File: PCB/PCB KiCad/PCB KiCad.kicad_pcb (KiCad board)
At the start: 2 copper layers, 80.1 x 120 mm, 78 parts, among them J1 Conn_01x04, J2 Conn_01x08, J3 Qwiic, J4 Conn_01x04, J5 Conn_01x04, SW1 MCU_RESET, SW2 TRIGGER, U1 OPA2376AID, U2 NAU7802SGI, U3 AMS1117-3.3, U4 TLC59208FIPWR

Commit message: typo
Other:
- board text added: "Plastic Scanner Development Board 2.3 May 2023"
- board text removed: "Plastic Scanner Development Board 2.2 April 2023"

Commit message: pre route
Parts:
- removed the ? at (119.0, 32.0)
- removed the ? at (47.0, 144.0)
- removed A1: Arduino_UNO_R3, Module:Arduino_UNO_R3
- removed C15: 22u, Capacitor_SMD:C_0805_2012Metric_Pad1.18x1.45mm_HandSolder
- removed C16: 100n, Capacitor_SMD:C_0805_2012Metric_Pad1.18x1.45mm_HandSolder
- removed D11: 1720nm, LED_SMD:LED_1206_3216Metric_Pad1.42x1.75mm_HandSolder
- removed D12: LED RED, LED_SMD:LED_0805_2012Metric_Pad1.15x1.40mm_HandSolder
- removed the D3 at (91.4, 33.4)
- removed the G*** at (118.9, 48.5)
- removed the G*** at (118.6, 40.5)
- removed the G*** at (83.4, 121.0)
- removed G1: LOGO, LOGO
- removed the J2 at (47.3, 119.2)
- removed R16, R17, R18, R19, R20, R21, R22: 47, Resistor_SMD:R_0805_2012Metric_Pad1.20x1.40mm_HandSolder
- removed the R7 at (88.2, 33.4)
- removed the R8 at (94.7, 33.4)
- removed REF**, e (x3): MountingHole_3.2mm_M3, MountingHole:MountingHole_3.2mm_M3
- removed SW1: MCU_RESET, Button_Switch_THT:SW_PUSH_6mm
- removed SW2: TRIGGER, Button_Switch_THT:SW_PUSH_6mm
- removed U4: TLC59208FIPWR, TLC59208:Texas_Instruments-TLC59208FIPWR-Level_A
- removed mouse-bite-2mm-slot (x6): VAL**, mousebites:mouse-bite-2mm-slot
- added ?: , , F.Cu at (97.9, 151.8)
- added ?: , , F.Cu at (67.9, 121.8)
- added ?: , , F.Cu at (67.9, 151.8)
- added C14: 100n, Capacitor_SMD:C_0805_2012Metric_Pad1.18x1.45mm_HandSolder, F.Cu at (65.2, 121.9)
- added D10: 1720nm, LED_SMD:LED_1206_3216Metric_Pad1.42x1.75mm_HandSolder, F.Cu at (78.4, 131.1)
- added H1: MountingHole, MountingHole:MountingHole_3.2mm_M3, F.Cu at (67.9, 121.8)
- added H2: MountingHole, MountingHole:MountingHole_3.2mm_M3, F.Cu at (67.9, 151.8)
- added H3: MountingHole, MountingHole:MountingHole_3.2mm_M3, F.Cu at (97.9, 151.8)
- added H4: MountingHole, MountingHole:MountingHole_3.2mm_M3, F.Cu at (97.9, 121.8)
- added J4: Conn_01x04, Connector_PinSocket_2.54mm:PinSocket_1x04_P2.54mm_Vertical, F.Cu at (65.2, 142.3)
- added R11: 47, Resistor_SMD:R_0805_2012Metric_Pad1.20x1.40mm_HandSolder, F.Cu at (96.0, 131.8)
- added R12: 47, Resistor_SMD:R_0805_2012Metric_Pad1.20x1.40mm_HandSolder, F.Cu at (96.0, 134.8)
- added R13: 47, Resistor_SMD:R_0805_2012Metric_Pad1.20x1.40mm_HandSolder, F.Cu at (96.0, 137.7)
- added R15: 47, Resistor_SMD:R_0805_2012Metric_Pad1.20x1.40mm_HandSolder, F.Cu at (96.0, 143.6)
- C1, C10, C11, C2, C3, C4, C5, C6, C7, C8, C9, FB1, R1, R2, R3, R4, R5, R6, U1, U2: moved to B.Cu
- C12: renamed from C14; moved to B.Cu
- C13: value 10u -> 22u
- D2: value LED BLUE -> LED RED; moved to B.Cu
- J2: renamed from J3; moved to B.Cu
- R10, R9: value 10k -> 47
- R14: value 1k -> 47
- R7: renamed from R11; moved to B.Cu
- U3: value AMS1117-3.3 -> TLC59208FIPWR; footprint Package_TO_SOT_SMD:SOT-223-3_TabPin2 -> TLC59208:Texas_Instruments-TLC59208FIPWR-Level_A; moved to B.Cu
- moved D2 114.2 mm to (65.3, 145.8), turned to -90 degrees
- moved G*** 99.8 mm to (197.9, 99.8)
- moved G*** 99.8 mm to (206.2, 100.1)
- moved R10 97.8 mm to (96.0, 128.8), turned to 0 degrees
- moved R9 94.4 mm to (96.0, 125.9), turned to 0 degrees
- moved C10 52.7 mm to (78.2, 147.2), turned to -90 degrees
- moved J2 51.9 mm to (75.1, 153.8), turned to 180 degrees
- moved U3 48.3 mm to (93.0, 137.6), turned to 180 degrees
- moved R7 47.9 mm to (67.8, 145.8), turned to -90 degrees
- moved R5 47.6 mm to (98.3, 147.1), turned to 0 degrees
- moved R6 45.1 mm to (98.3, 145.0), turned to 0 degrees
- moved C6 44.2 mm to (95.3, 146.0), turned to 90 degrees
- moved U2 43.6 mm to (84.2, 150.7), turned to 180 degrees
- moved FB1 43.6 mm to (75.8, 147.2), turned to -90 degrees
- moved C7 42.8 mm to (92.8, 146.0), turned to 90 degrees
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- renumbered D4 to D3, D5 to D4, D6 to D5, D7 to D6, D8 to D7, D9 to D8, D10 to D9, J4 to J3, R15 to R8
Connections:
- C13 pad 1: 5v_RAW -> 3.3v
- D4 pad 1: Net-(D5-K) -> Net-(D4-K)
- D5 pad 1: Net-(D6-K) (its old number) -> Net-(D5-K)
- D9 pad 1: Net-(D10-K) -> Net-(D9-K)
- R10 pad 1: 5v_RAW -> LED3
- R10 pad 2: TRIGGER -> Net-(D5-K)
- R14 pad 1: LED_RESET -> LED7
- R14 pad 2: 3.3v -> Net-(D9-K)
- R7 pad 2: Net-(D12-A) -> Net-(D2-A)
- R9 pad 1: 5v_RAW -> LED2
- R9 pad 2: MCU_RESET -> Net-(D4-K)
- U2 pad 12: DRDY_INT -> unconnected-(U2-DRDY-Pad12)
- U3 pad 2: 3v3unf -> GND
- U3 pad 3: 5v_RAW -> GND
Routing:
- net 3.3v: track 188.8 -> 0.00 mm, vias 4 -> 0
- net TRIGGER: track 181.8 -> 0.00 mm, vias 1 -> 0
- net DRDY_INT: track 161.4 -> 0.00 mm, vias 1 -> 0
- net LED_RESET: track 161.2 -> 0.00 mm, vias 1 -> 0
- net SCL: track 157.3 -> 0.00 mm, vias 1 -> 0
- net 5v_RAW: track 153.1 -> 0.00 mm, vias 3 -> 0
- net SDA: track 146.1 -> 0.00 mm, vias 1 -> 0
- net LED_BLUE: track 60.5 -> 0.00 mm, vias 1 -> 0
- net LED8: track 58.6 -> 0.00 mm, vias 1 -> 0
- net LED7: track 58.2 -> 0.00 mm, vias 1 -> 0
- net LED6: track 57.8 -> 0.00 mm, vias 1 -> 0
- net LED5: track 56.9 -> 0.00 mm, vias 1 -> 0
- net /ADC/AIN+: track 40.8 -> 0.00 mm, vias 2 -> 0
- net 3v3unf: track 40.7 -> 0.00 mm
- net /Sensor/A+: track 37.9 -> 0.00 mm
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- removed copper zone on B.Cu, net GND
- removed copper zone on F.Cu, net GND
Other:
- board size 80.1 x 120 mm -> 40 x 40 mm
- board text removed: "Act"
- board text removed: "GND 3.3V SDA SCL LED RST DRDY TRIG 5V raw"
- board text removed: "JLCJLCJLCJLC"
- board text removed: "Power"
- board text removed: "Reset"
- board text removed: "Trigger"

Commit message: routed!
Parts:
- removed ? (x3): , 
- removed H3: MountingHole, MountingHole:MountingHole_3.2mm_M3
- C13, C14: moved to B.Cu
- D1: footprint Diode_SMD:D_1206_3216Metric_Pad1.42x1.75mm_HandSolder -> Diode_THT:D_A-405_P2.54mm_Vertical_KathodeUp
- moved H2 41.8 mm to (95.0, 120.0)
- moved C13 33.8 mm to (69.0, 152.0), turned to 90 degrees
- moved R15 32.8 mm to (66.0, 130.4)
- moved R12 30.9 mm to (66.0, 142.0)
- moved R14 30.7 mm to (66.0, 134.3)
- moved R13 30.0 mm to (66.0, 138.1)
- moved H4 28.3 mm to (95.0, 150.0)
- moved U3 21.1 mm to (71.9, 136.7)
- moved J2 14.1 mm to (63.1, 146.6), turned to 90 degrees
- moved C10 12.5 mm to (66.7, 152.0), turned to 90 degrees
- moved FB1 12.4 mm to (64.4, 152.1), turned to 90 degrees
- moved D2 11.8 mm to (75.4, 152.0), turned to 90 degrees
- moved R11 10.4 mm to (93.9, 142.0), turned to 180 degrees
- moved C14 10.1 mm to (68.8, 131.3), turned to 90 degrees
- moved R10 9.50 mm to (93.9, 138.1), turned to 180 degrees
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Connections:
- R7 pad 1: 3v3unf -> 3.3v
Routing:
- net 3.3v: track 0.00 -> 184.9 mm
- net /ADC/AIN-: track 0.00 -> 40.4 mm
- net SDA: track 0.00 -> 39.7 mm
- net /ADC/AIN+: track 0.00 -> 39.1 mm
- net /Sensor/A-: track 0.00 -> 30.9 mm
- net /Sensor/A+: track 0.00 -> 30.9 mm
- net LED1: track 0.00 -> 28.2 mm
- net SCL: track 0.00 -> 27.6 mm
- net LED4: track 0.00 -> 27.2 mm
- net LED2: track 0.00 -> 26.9 mm
- net LED3: track 0.00 -> 25.9 mm
- net Net-(U2-REFN): track 0.00 -> 22.7 mm
- net GND: track 0.00 -> 18.4 mm, vias 0 -> 21
- net Net-(U1-OUT_A): track 0.00 -> 16.0 mm
- net Net-(U1-OUT_B): track 0.00 -> 15.3 mm
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- added copper zone on B.Cu, net GND
- added copper zone on F.Cu, net GND

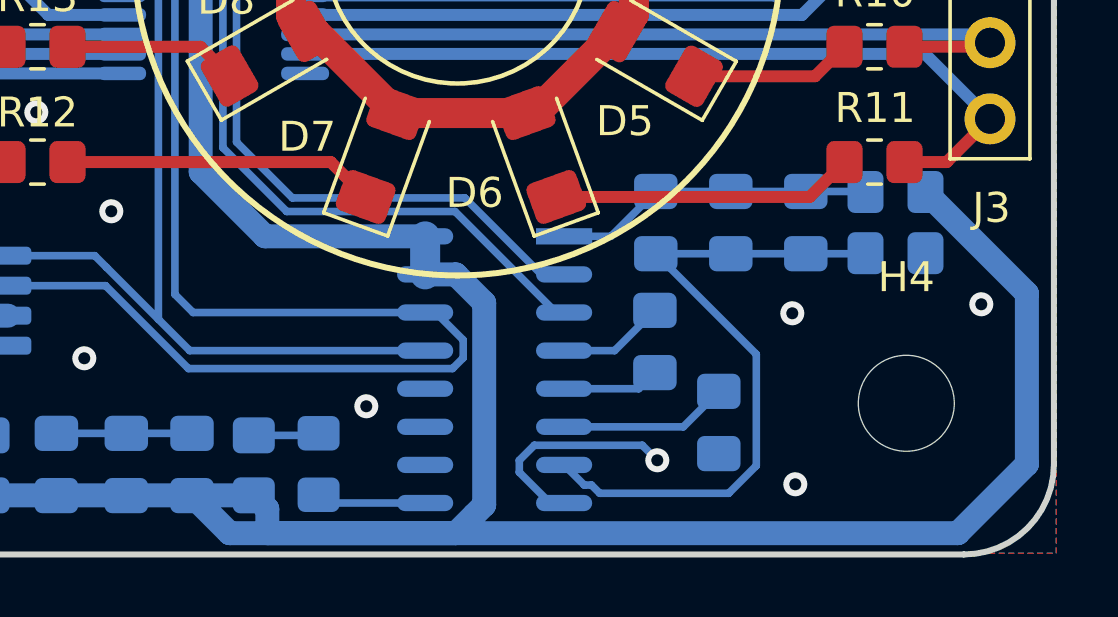
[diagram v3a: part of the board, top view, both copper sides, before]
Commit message: adds LP5951MFX
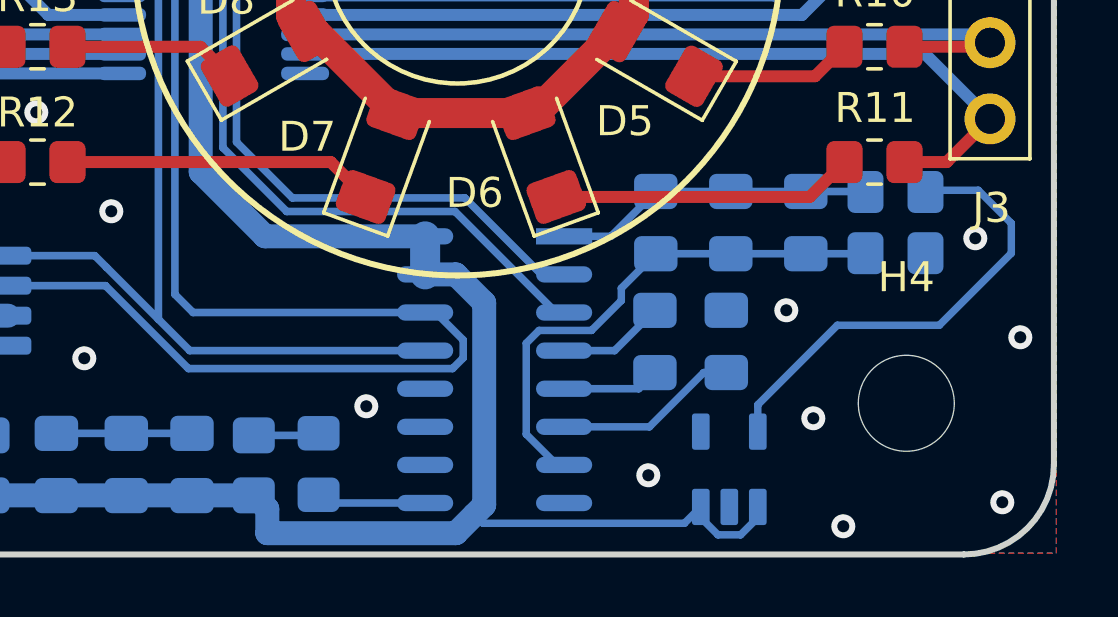
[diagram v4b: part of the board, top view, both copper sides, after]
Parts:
- added U4: LP5951MFX-1.8_NOPB, LP5951MFX-1.8_NOPB:SOT95P280X145-5N, B.Cu at (89.1, 152.2)
- moved C11 2.71 mm to (89.0, 147.9), turned to -90 degrees
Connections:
- R6 pad 2: 3.3v -> Net-(U4-VOUT)
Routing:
- net 3.3v: track 184.9 -> 156.1 mm
- net Net-(U4-VOUT): track 0.00 -> 15.8 mm
- net GND: track 18.4 -> 11.1 mm, vias 21 -> 24
- net Net-(U2-REFN): track 22.7 -> 17.6 mm
- net Net-(U2-VBG): track 5.65 -> 6.16 mm

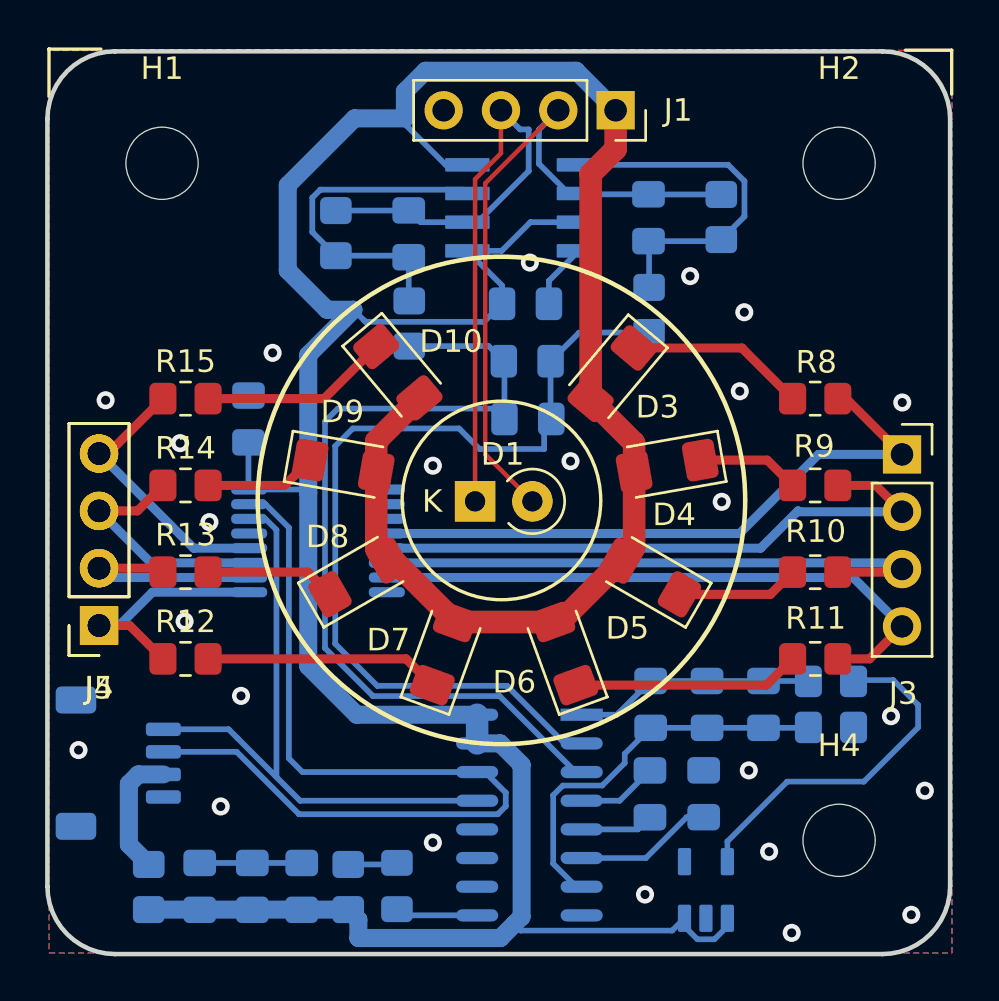
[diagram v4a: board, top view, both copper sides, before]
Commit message: square pcb
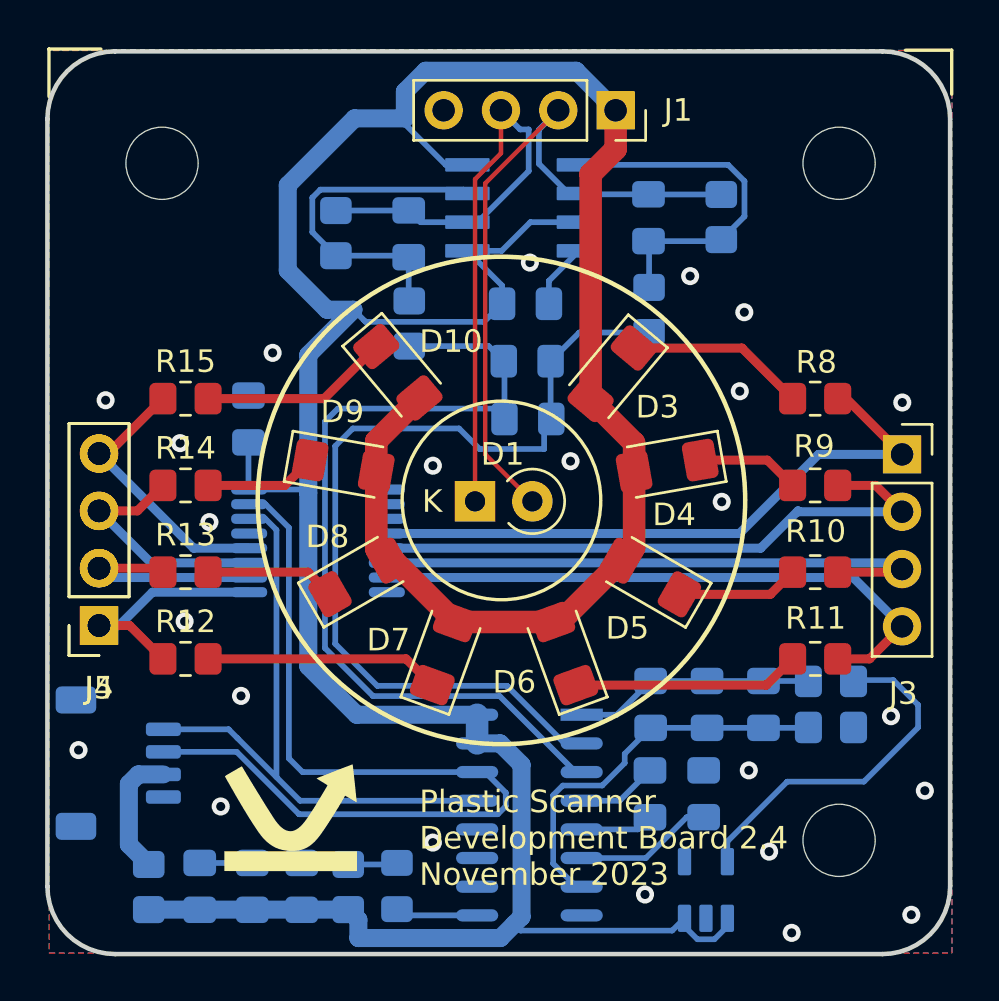
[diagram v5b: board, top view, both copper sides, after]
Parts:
- G***: moved to F.Cu
- moved G*** 141.4 mm to (64.6, 126.3)
- moved G*** 134.2 mm to (70.7, 148.8), turned to 0 degrees
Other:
- board text added: "Plastic Scanner Development Board 2.4 November 2023"
- board text removed: "Plastic Scanner Development Board 2.3 May 2023"
- board text removed: "S/N"
